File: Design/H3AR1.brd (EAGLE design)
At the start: 50.8 x 45.6 mm, 8 parts, among them P1 HEXABIT__REVERSED_NO_P3, U1 TPS76433DBVT

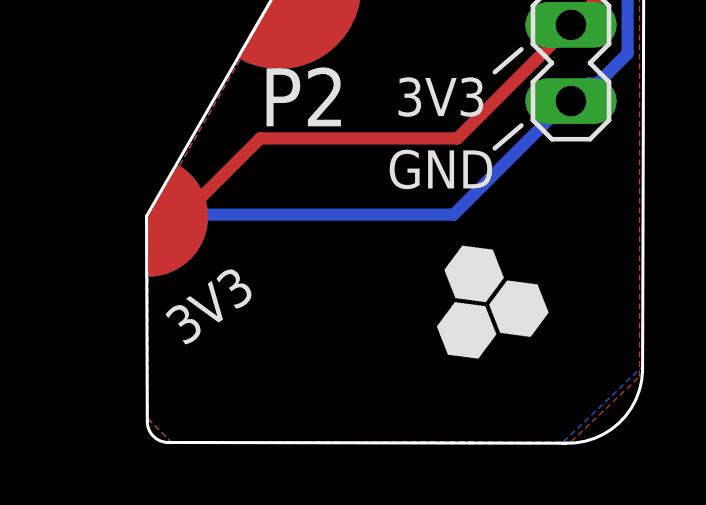
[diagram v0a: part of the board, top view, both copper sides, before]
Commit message: Update the logo
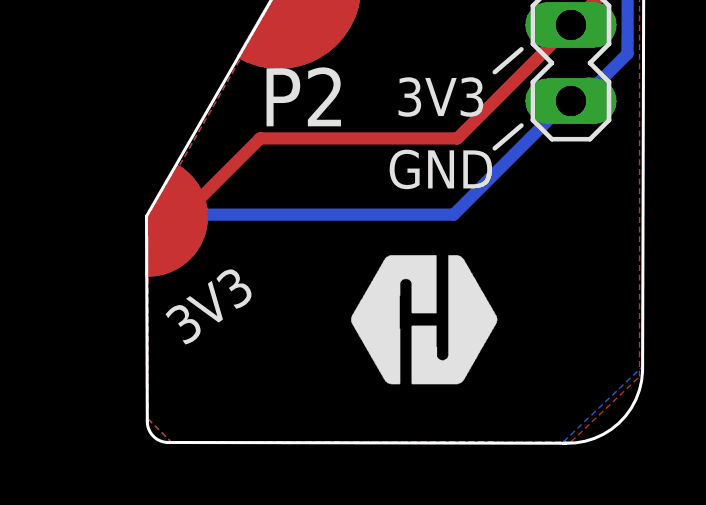
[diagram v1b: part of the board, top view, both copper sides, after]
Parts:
- added TRIMBLE-LOGO1: HEXA-LOGO, HEXABITZ_USER_INTERFACE_PARTS:HEXA-LOGO
